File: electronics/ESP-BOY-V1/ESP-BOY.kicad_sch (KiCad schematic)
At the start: 31 parts

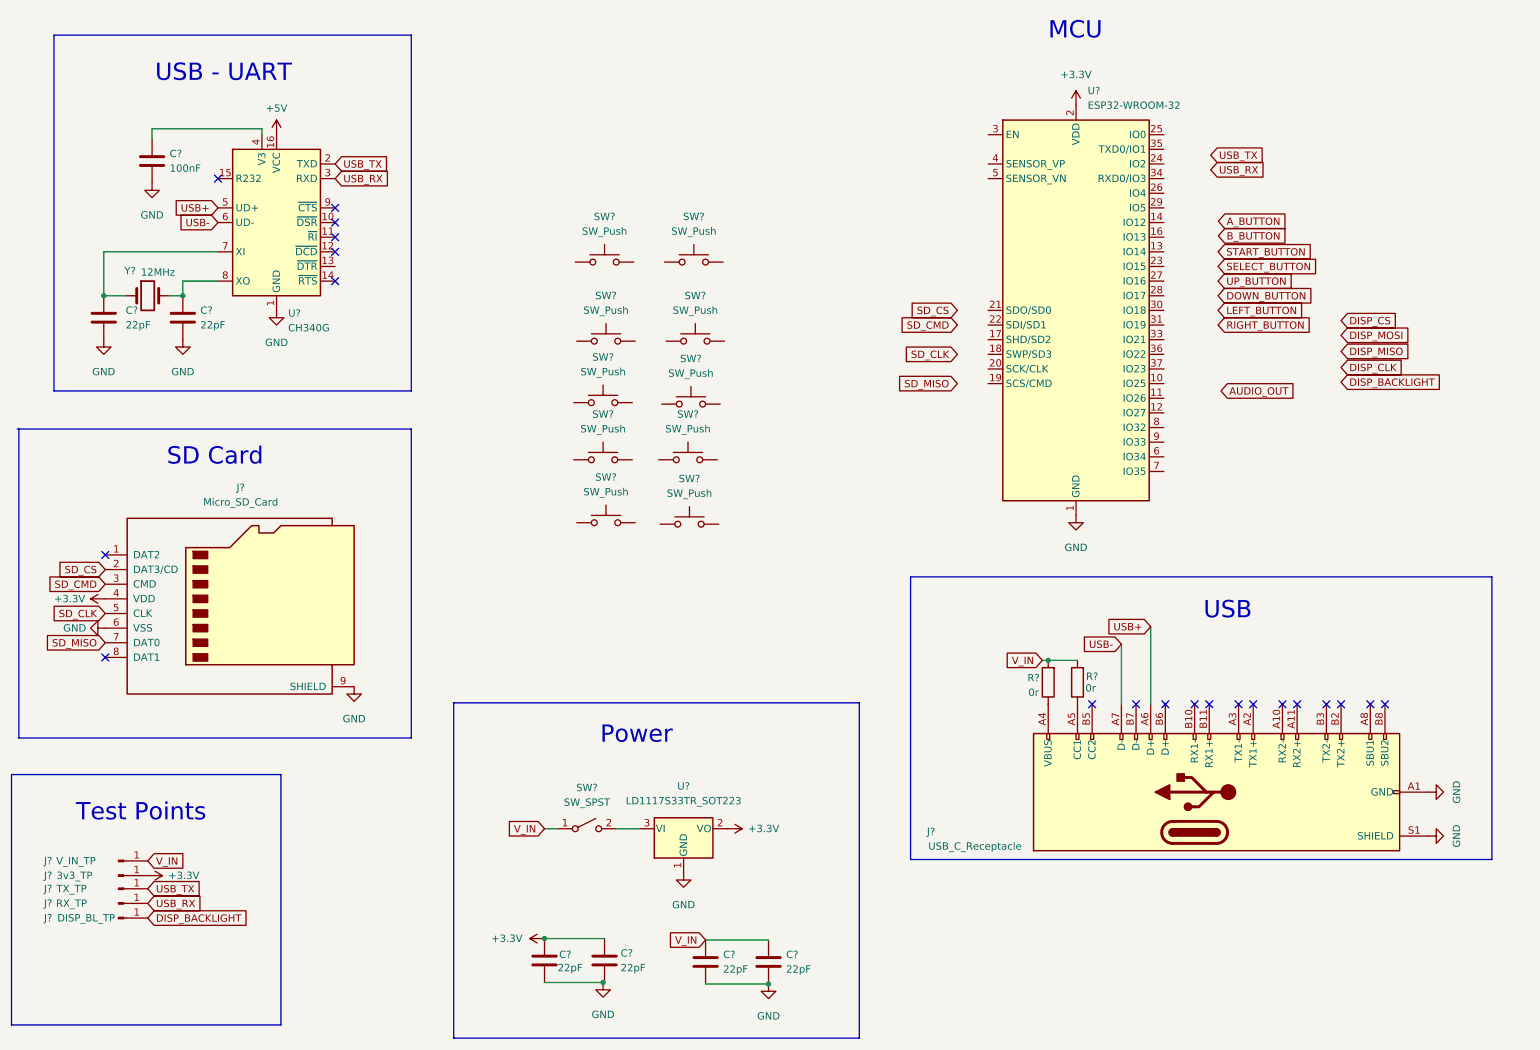
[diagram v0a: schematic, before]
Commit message: finish schematic connections
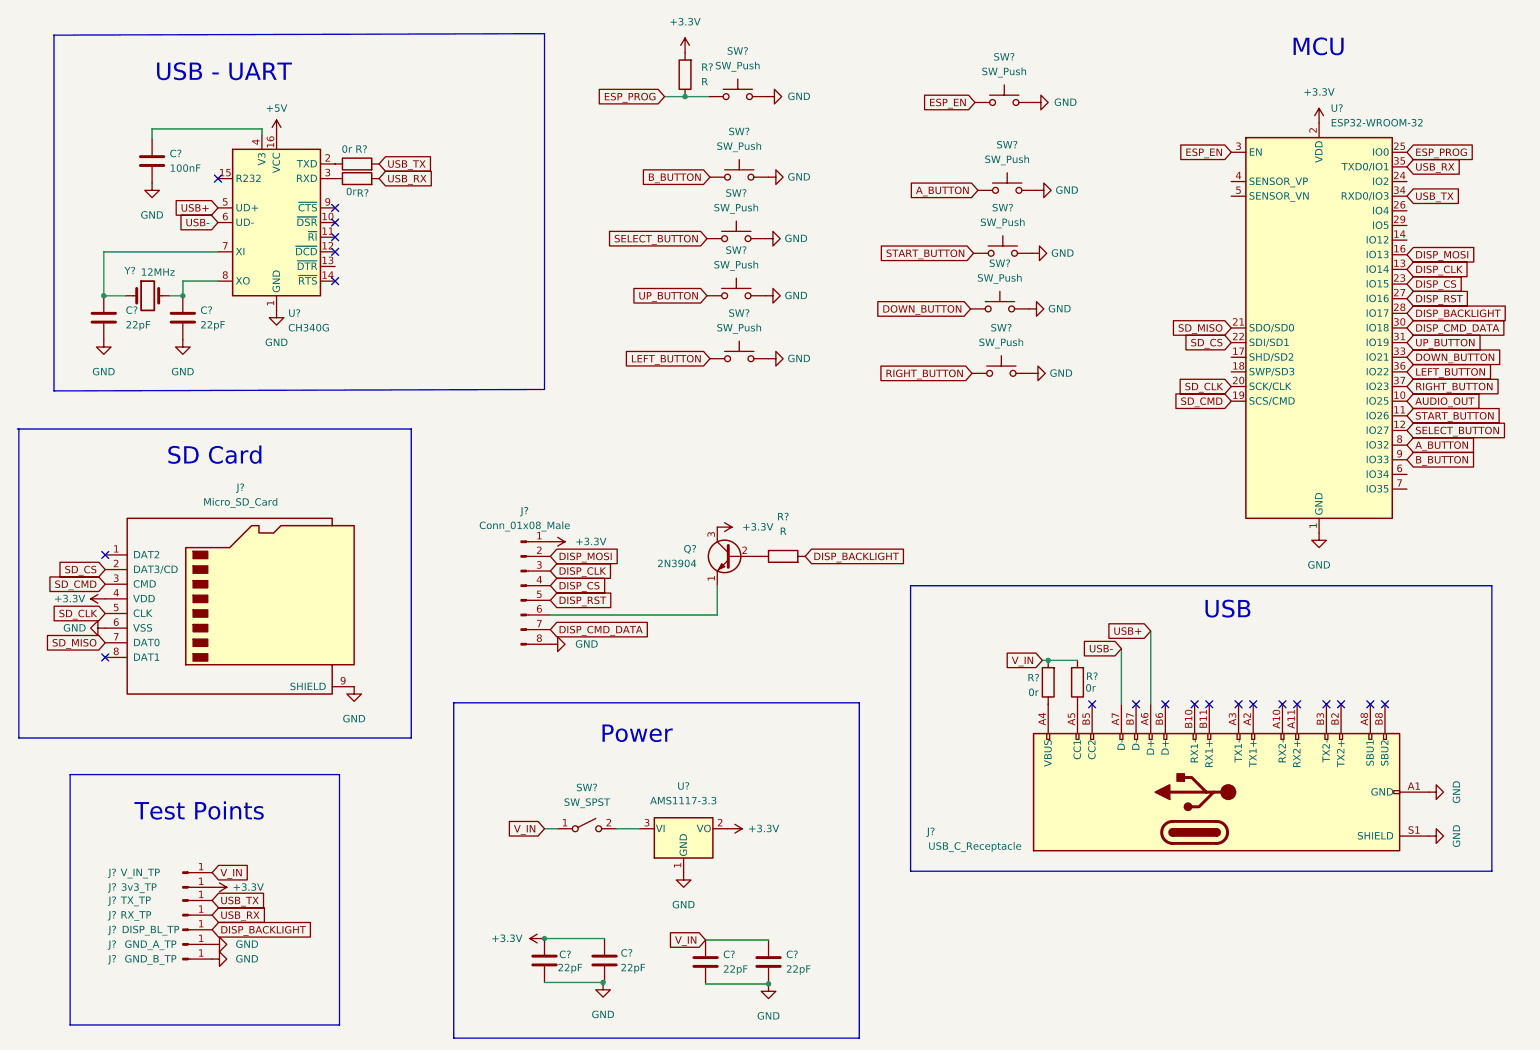
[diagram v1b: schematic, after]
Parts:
- removed U?: LD1117S33TR_SOT223, Package_TO_SOT_SMD:TO-252-2, symbol Regulator_Linear:LD1117S33TR_SOT223
- added J?: GND_A_TP, symbol Connector:Conn_01x01_Male
- added J?: GND_B_TP, symbol Connector:Conn_01x01_Male
- added J?: Conn_01x08_Male, symbol Connector:Conn_01x08_Male
- added Q?: 2N3904, Package_TO_SOT_THT:TO-92_Inline, symbol Transistor_BJT:2N3904
- added R? (x2): 0r, symbol Device:R
- added R? (x2): R, symbol Device:R
- added U?: AMS1117-3.3, Package_TO_SOT_SMD:SOT-223-3_TabPin2, symbol Regulator_Linear:AMS1117-3.3
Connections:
- net +3V3: now also J?.1 (Pin_1), Q?.3 (C), R?.2, U?.2 (VO)
- net AUDIO_OUT: now also U?.10 (IO25)
- net A_BUTTON: now also SW?.1, U?.8 (IO32)
- net B_BUTTON: now also SW?.1, U?.9 (IO33)
- net DISP_BACKLIGHT: now also U?.28 (IO17), R?.2
- net DISP_CLK: now also U?.13 (IO14), J?.3 (Pin_3)
- net DISP_CS: now also U?.23 (IO15), J?.4 (Pin_4)
- net DISP_MOSI: now also U?.16 (IO13), J?.2 (Pin_2)
- net DOWN_BUTTON: now also SW?.1, U?.33 (IO21)
- net GND: now also SW?.2, SW?.2, SW?.2, SW?.2, SW?.2, SW?.2, SW?.2, SW?.2, SW?.2, SW?.2, J?.1 (Pin_1), J?.1 (Pin_1), J?.8 (Pin_8), U?.1 (GND)
- net LEFT_BUTTON: now also SW?.1, U?.36 (IO22)
- net RIGHT_BUTTON: now also SW?.1, U?.37 (IO23)
- net SD_CLK: now also U?.20 (SCK/CLK)
- net SD_CMD: now also U?.19 (SCS/CMD)
- net SD_CS: now also U?.22 (SDI/SD1)
- net SD_MISO: now also U?.21 (SDO/SD0)
- net SELECT_BUTTON: now also SW?.1, U?.12 (IO27)
- net START_BUTTON: now also SW?.1, U?.11 (IO26)
- net UP_BUTTON: now also SW?.1, U?.31 (IO19)
- net USB_RX: now also U?.35 (TXD0/IO1), R?.2; no longer U?.3 (RXD)
- net USB_TX: now also U?.34 (RXD0/IO3), R?.2; no longer U?.2 (TXD)
- net ESP_EN: now reaches SW?.1
- net ESP_EN: now also U?.3 (EN)
- net ESP_PROG: now reaches U?.25 (IO0)
- net ESP_PROG: now also SW?.1, R?.1
- net DISP_RST: now reaches U?.27 (IO16)
- net DISP_RST: now also J?.5 (Pin_5)
- net DISP_CMD_DATA: now reaches U?.30 (IO18)
- net DISP_CMD_DATA: now also J?.7 (Pin_7)
- net at SW?.2 (B): now also U?.3 (VI)
- new net: R?.1, U?.2 (TXD)
- new net: R?.1, U?.3 (RXD)
- new net: Q?.2 (B), R?.1
- new net: J?.6 (Pin_6), Q?.1 (E)
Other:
- moved on the sheet: J?, SW?, U?
